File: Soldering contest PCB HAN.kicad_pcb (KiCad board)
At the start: 2 copper layers, 99.1 x 98.6 mm, 17 parts, among them J1 Screw_Terminal_01x02, Q1 2N3904, Q2 2N3904

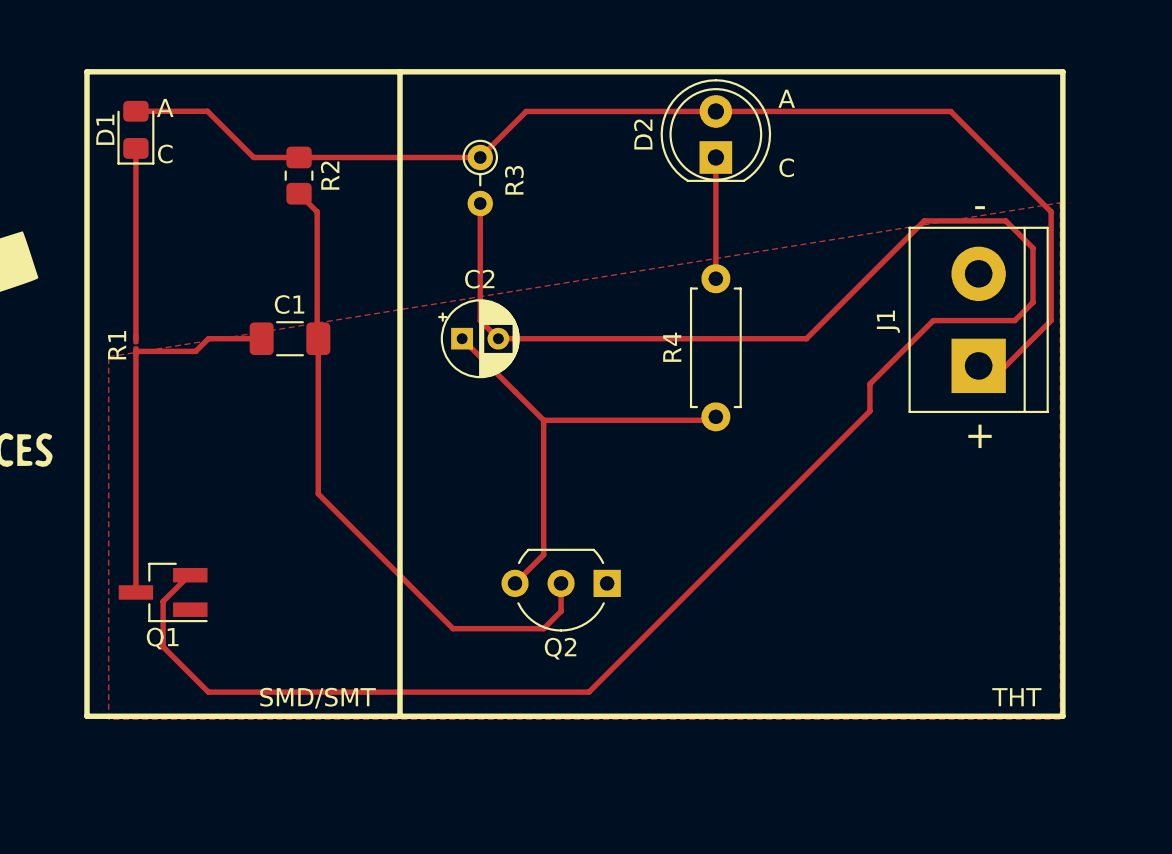
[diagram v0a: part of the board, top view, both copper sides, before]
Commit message: changed terminal position
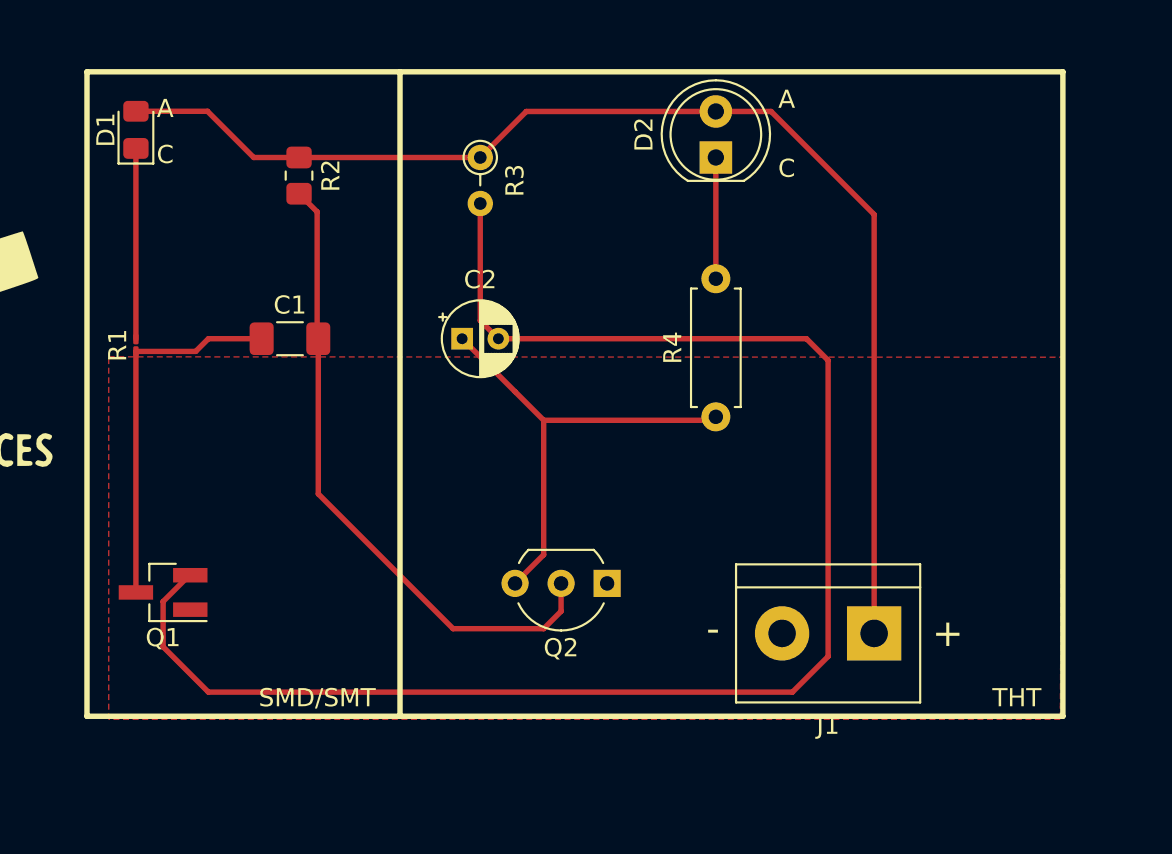
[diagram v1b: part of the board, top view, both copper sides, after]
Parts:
- moved J1 15.8 mm to (177.0, 111.8), turned to 180 degrees
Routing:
- net Net-(C2-Pad2): track 107.1 -> 86.0 mm
- net Net-(D1-Pad2): track 65.9 -> 68.3 mm
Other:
- board text added: "TIPS: -Wear safety goggles -Avoid breathing in the solder fumes -Use the appropriate soldering tip for the job -350°C-400°C are usual soldering temperatures -{dblquote}Pre tin{dblquote} components/wires -Heat the pad and the component while adding tin -Use a helping hand or board clamp -Pliers make handling small components easier -Solder paste requires around 220°C to melt -Low melt solder/hot a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"
- board text removed: "TIPS: -Wear safety goggles -Avoid breathing in the solder fumes -350°C-400°C are usual soldering temperatures -{dblquote}Pre tin{dblquote} components/wires -Heat the pad and the component while adding tin -Use a helping hand or board clamp -Pliers make handling small components easier -Solder paste requires around 220°C to melt -Low melt solder/hot air is the easiest way to remove components with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"
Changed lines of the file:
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@@
   )
   (footprint "TerminalBlock:TerminalBlock_bornier-2_P5.08mm" (layer "F.Cu")
-    (at 182.804 97 90)
+    (at 177.038 111.76 180)
     (descr "simple 2-pin terminal block, pitch 5.08mm, revamped version of bornier2")
     (tags "terminal block bornier2")
@@
     (property "Sheetname" "")
     (attr through_hole)
-    (fp_text reference "J1" (at 2.54 -5.08 90) (layer "F.SilkS")
+    (fp_text reference "J1" (at 2.54 -5.08) (layer "F.SilkS")
       (effects (font (size 1 1) (thickness 0.15)))
     )
-    (fp_text value "Screw_Terminal_01x02" (at 2.54 5.08 90) (layer "F.Fab")
+    (fp_text value "Screw_Terminal_01x02" (at 2.54 5.08) (layer "F.Fab")
       (effects (font (size 1 1) (thickness 0.15)))
     )
-    (fp_text user "${REFERENCE}" (at 2.54 0 90) (layer "F.Fab")
+    (fp_text user "${REFERENCE}" (at 2.54 0) (layer "F.Fab")
       (effects (font (size 1 1) (thickness 0.15)))
     )
@@
     (fp_line (start -2.46 3.75) (end 7.54 3.75) (layer "F.Fab") (width 0.1))
     (fp_line (start 7.54 3.75) (end 7.54 -3.75) (layer "F.Fab") (width 0.1))
-    (pad "1" thru_hole rect (at 0 0 90) (size 3 3) (drill 1.52) (layers *.Cu *.Mask)
+    (pad "1" thru_hole rect (at 0 0 180) (size 3 3) (drill 1.52) (layers *.Cu *.Mask)
       (net 6 "Net-(D1-Pad2)") (pinfunction "Pin_1") (pintype "passive"))
-    (pad "2" thru_hole circle (at 5.08 0 90) (size 3 3) (drill 1.52) (layers *.Cu *.Mask)
+    (pad "2" thru_hole circle (at 5.08 0 180) (size 3 3) (drill 1.52) (layers *.Cu *.Mask)
       (net 8 "GND") (pinfunction "Pin_2") (pintype "passive"))
     (model "${KICAD6_3DMODEL_DIR}/TerminalBlock.3dshapes/TerminalBlock_bornier-2_P5.08mm.wrl"
@@
   (gr_arc (start 205.486 51.301321) (mid 208.90322 52.71678) (end 210.318679 56.134) (layer "Edge.Cuts") (width 0.1))
   (gr_line (start 210.318679 56.134) (end 210.312 149.86) (layer "Edge.Cuts") (width 0.1))
-  (gr_text "TIPS:\n-Wear safety goggles\n-Avoid breathing in the solder fumes\n-350°C-400°C are usual soldering temperatures\n-{dblquote}Pre tin{dblquote} components/wires\n-Heat the pad and the component while adding tin\n-Use a helping hand or board clamp\n-Pliers make handling small components easier\n-Solder paste requires around 220°C to melt\n-Low melt solder/hot air is the easiest way to remove \n components with many pins\n-Dull solder joints aren't great\n" (at 208.788 72.644) (layer "B.SilkS")
+  (gr_text "TIPS:\n-Wear safety goggles\n-Avoid breathing in the solder fumes\n-Use the appropriate soldering tip for the job\n-350°C-400°C are usual soldering temperatures\n-{dblquote}Pre tin{dblquote} components/wires\n-Heat the pad and the component while adding tin\n-Use a helping hand or board clamp\n-Pliers make handling small components easier\n-Solder paste requires around 220°C to melt\n-Low melt solder/hot air is the easiest way to remove \n components with many pins\n-Avoid dull looking solder joints\n" (at 208.788 72.644) (layer "B.SilkS")
     (effects (font (size 1.2 1.2) (thickness 0.17)) (justify left mirror))
   )
@@
     (effects (font (size 1 1) (thickness 0.15)))
   )
-  (gr_text "-" (at 182.88 88.138) (layer "F.SilkS")
+  (gr_text "-" (at 168.148 111.506) (layer "F.SilkS")
     (effects (font (size 1.5 1.5) (thickness 0.2)))
   )
@@
     (effects (font (size 2 2) (thickness 0.3)))
   )
-  (gr_text "+\n" (at 182.88 100.838) (layer "F.SilkS")
+  (gr_text "+\n" (at 181.102 111.76) (layer "F.SilkS")
     (effects (font (size 1.5 1.5) (thickness 0.2)))
   )
@@
   (segment (start 158.804 100) (end 157.224 98.42) (width 0.3) (layer "F.Cu") (net 3))
   (segment (start 157.224 109) (end 158.804 107.42) (width 0.3) (layer "F.Cu") (net 3))
+  (segment (start 140.304 115) (end 137.804 112.5) (width 0.3) (layer "F.Cu") (net 4))
+  (segment (start 137.804 112.5) (end 137.804 110) (width 0.3) (layer "F.Cu") (net 4))
+  (segment (start 174.498 113.03) (end 172.528 115) (width 0.3) (layer "F.Cu") (net 4))
+  (segment (start 137.804 110) (end 139.254 108.55) (width 0.3) (layer "F.Cu") (net 4))
+  (segment (start 173.304 95.5) (end 174.498 96.694) (width 0.3) (layer "F.Cu") (net 4))
+  (segment (start 139.254 108.55) (end 139.304 108.55) (width 0.3) (layer "F.Cu") (net 4))
+  (segment (start 172.528 115) (end 140.304 115) (width 0.3) (layer "F.Cu") (net 4))
   (segment (start 156.304 95.5) (end 173.304 95.5) (width 0.3) (layer "F.Cu") (net 4))
-  (segment (start 185.804 93.5) (end 184.804 94.5) (width 0.3) (layer "F.Cu") (net 4))
-  (segment (start 139.254 108.55) (end 139.304 108.55) (width 0.3) (layer "F.Cu") (net 4))
-  (segment (start 184.804 94.5) (end 180.304 94.5) (width 0.3) (layer "F.Cu") (net 4))
-  (segment (start 180.304 94.5) (end 176.804 98) (width 0.3) (layer "F.Cu") (net 4))
-  (segment (start 184.304 89) (end 185.804 90.5) (width 0.3) (layer "F.Cu") (net 4))
-  (segment (start 176.804 98) (end 176.804 99.5) (width 0.3) (layer "F.Cu") (net 4))
-  (segment (start 173.304 95.5) (end 179.804 89) (width 0.3) (layer "F.Cu") (net 4))
-  (segment (start 176.804 99.5) (end 161.304 115) (width 0.3) (layer "F.Cu") (net 4))
-  (segment (start 140.304 115) (end 137.804 112.5) (width 0.3) (layer "F.Cu") (net 4))
   (segment (start 155.304 88.04) (end 155.304 94.5) (width 0.3) (layer "F.Cu") (net 4))
-  (segment (start 185.804 90.5) (end 185.804 93.5) (width 0.3) (layer "F.Cu") (net 4))
   (segment (start 155.304 94.5) (end 156.304 95.5) (width 0.3) (layer "F.Cu") (net 4))
-  (segment (start 137.804 110) (end 139.254 108.55) (width 0.3) (layer "F.Cu") (net 4))
-  (segment (start 161.304 115) (end 140.304 115) (width 0.3) (layer "F.Cu") (net 4))
-  (segment (start 179.804 89) (end 184.304 89) (width 0.3) (layer "F.Cu") (net 4))
-  (segment (start 137.804 112.5) (end 137.804 110) (width 0.3) (layer "F.Cu") (net 4))
+  (segment (start 174.498 96.694) (end 174.498 113.03) (width 0.3) (layer "F.Cu") (net 4))
   (segment (start 136.304 95.525) (end 136.304 85) (width 0.3) (layer "F.Cu") (net 5))
+  (segment (start 171.352 82.96) (end 177.038 88.646) (width 0.3) (layer "F.Cu") (net 6))
   (segment (start 145.304 85.5) (end 155.304 85.5) (width 0.3) (layer "F.Cu") (net 6))
   (segment (start 157.844 82.96) (end 155.304 85.5) (width 0.3) (layer "F.Cu") (net 6))
-  (segment (start 168.304 82.96) (end 181.264 82.96) (width 0.3) (layer "F.Cu") (net 6))
-  (segment (start 184.304 97) (end 182.804 97) (width 0.3) (layer "F.Cu") (net 6))
+  (segment (start 168.304 82.96) (end 171.352 82.96) (width 0.3) (layer "F.Cu") (net 6))
   (segment (start 168.304 82.96) (end 157.844 82.96) (width 0.3) (layer "F.Cu") (net 6))
   (segment (start 142.804 85.5) (end 145.304 85.5) (width 0.3) (layer "F.Cu") (net 6))
-  (segment (start 186.804 94.5) (end 184.304 97) (width 0.3) (layer "F.Cu") (net 6))
-  (segment (start 181.264 82.96) (end 186.804 88.5) (width 0.3) (layer "F.Cu") (net 6))
+  (segment (start 177.038 88.646) (end 177.038 111.76) (width 0.3) (layer "F.Cu") (net 6))
   (segment (start 140.254 82.95) (end 142.804 85.5) (width 0.3) (layer "F.Cu") (net 6))
-  (segment (start 186.804 88.5) (end 186.804 94.5) (width 0.3) (layer "F.Cu") (net 6))
   (segment (start 136.304 82.95) (end 140.254 82.95) (width 0.3) (layer "F.Cu") (net 6))
   (segment (start 168.304 92.19) (end 168.304 85.5) (width 0.3) (layer "F.Cu") (net 7))
@@
     (connect_pads (clearance 0.508))
     (min_thickness 0.254) (filled_areas_thickness no)
-    (fill yes (thermal_gap 0.508) (thermal_bridge_width 0.508))
+    (fill (thermal_gap 0.508) (thermal_bridge_width 0.508))
     (polygon
       (pts
@@
         (xy 134.804 116.5)
         (xy 134.804 96.5)
-        (xy 187.304 88)
+        (xy 187.452 96.52)
       )
     )

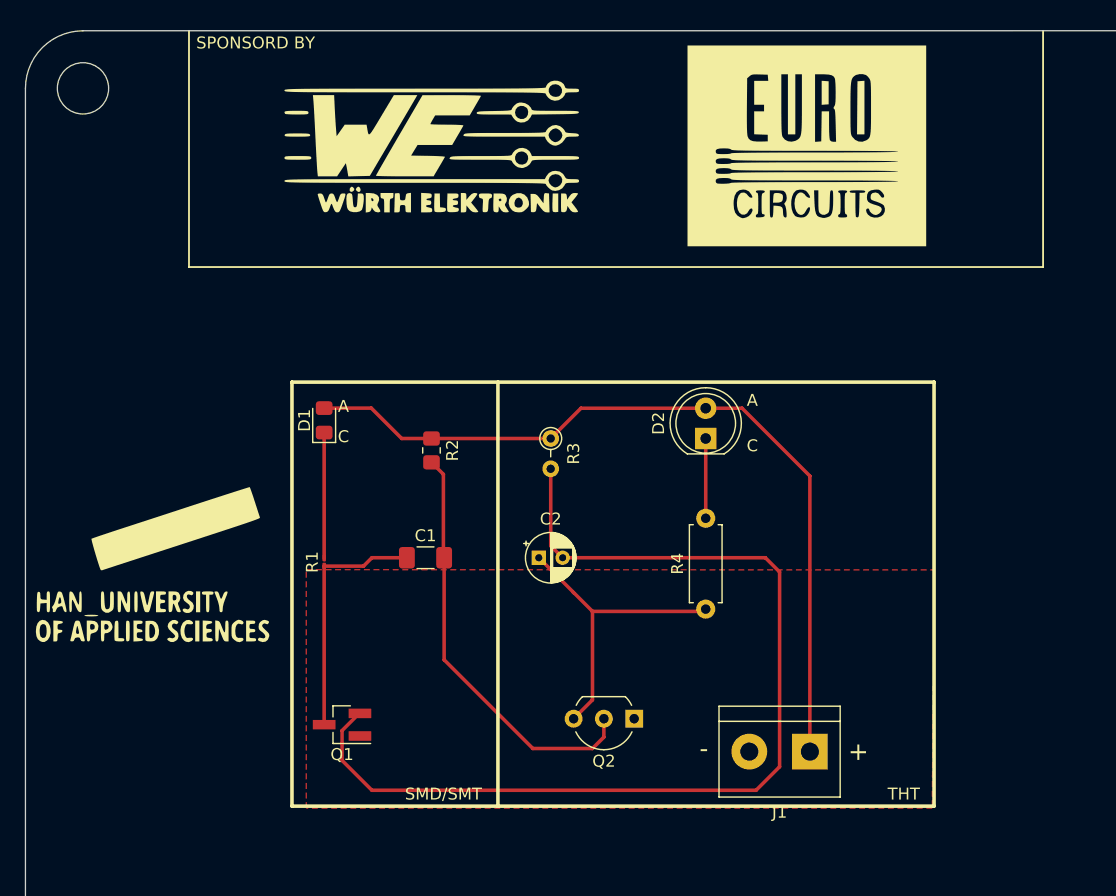
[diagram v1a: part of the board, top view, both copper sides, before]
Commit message: incorporated Remko's feedback
-added Romex logo
-added text: "Designed for: ESE-day 27 January 2023 soldering contest"
-moved terminal to mid bottom to balance weight
-
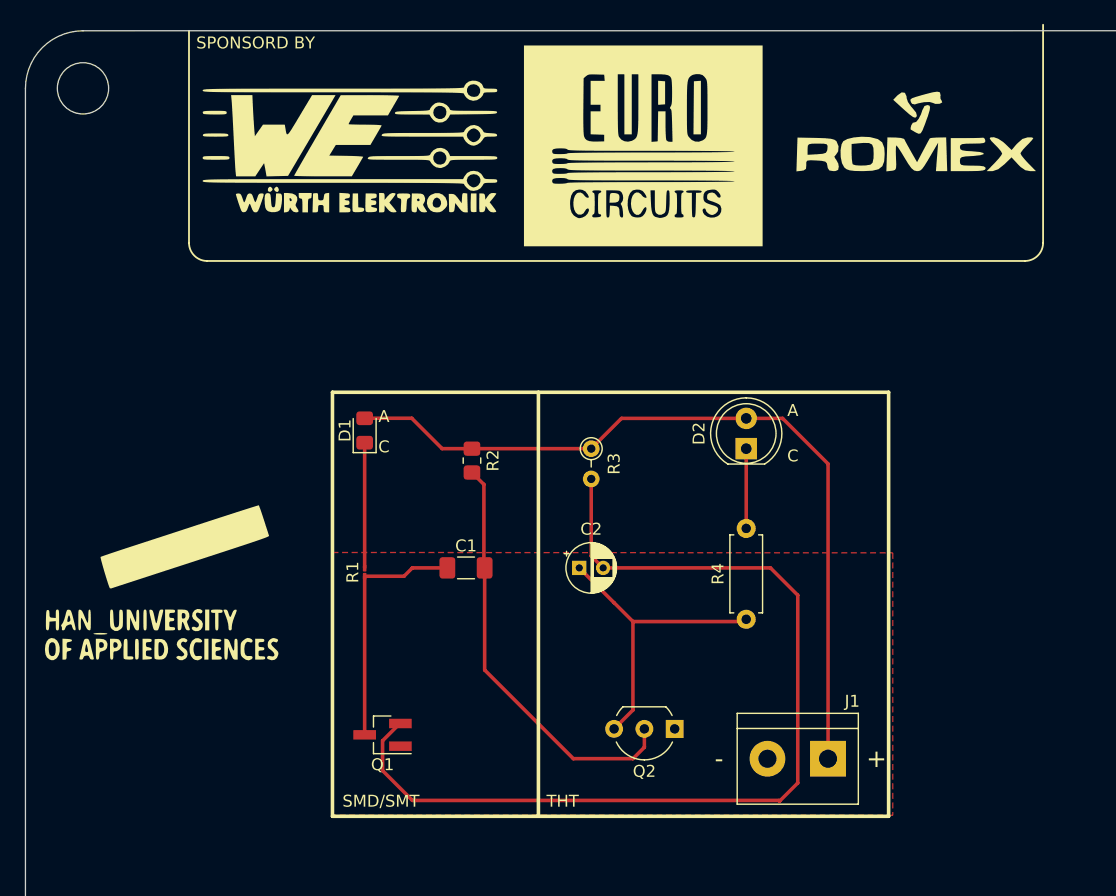
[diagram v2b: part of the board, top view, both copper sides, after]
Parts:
- added G***: LOGO, LOGO, F.Cu at (185.9, 59.7)
- moved G*** 13.7 mm to (163.1, 61.0)
- moved G*** 6.86 mm to (138.4, 61.0)
- moved C1 3.50 mm to (148.2, 96.4)
- moved C2 3.50 mm to (157.7, 96.4)
- moved D1 3.50 mm to (139.7, 84.8)
- moved D2 3.50 mm to (171.7, 86.4)
- moved Q1 3.50 mm to (141.2, 110.4)
- moved Q2 3.50 mm to (165.7, 109.9)
- moved R1 3.50 mm to (139.7, 96.7)
- moved R2 3.50 mm to (148.7, 87.4)
- moved R3 3.50 mm to (158.7, 86.4)
- moved R4 3.50 mm to (171.7, 100.7)
- moved G*** 1.70 mm to (122.7, 97.5)
- moved J1 1.64 mm to (178.6, 112.4)
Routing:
- net Net-(C2-Pad2): track 86.0 -> 82.0 mm
- net Net-(D1-Pad2): track 68.3 -> 67.3 mm
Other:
- board text added: "Project: Astable multivibrator Version: 0.1 Date: 18-11-2022 Designed for: ESE-day 27 January 2023 soldering contest Designed by: Casper R. Tak"
- board text removed: "Project: Astable multivibrator (soldering contest) Version: 0.1 Date: 18-11-2022 Designed by: Casper R. Tak"

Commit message: removed tips, added ESE txt
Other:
- board text added: "EMBEDDED SYSTEMS ENGINEERING"
- board text removed: "TIPS: -Wear safety goggles -Avoid breathing in the solder fumes -Use the appropriate soldering tip for the job -350°C-400°C are usual soldering temperatures -{dblquote}Pre tin{dblquote} components/wires -Heat the pad and the component while adding tin -Use a helping hand or board clamp -Pliers make handling small components easier -Solder paste requires around 220°C to melt -Low melt solder/hot a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"
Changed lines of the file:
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@@
   (gr_arc (start 205.486 51.301321) (mid 208.90322 52.71678) (end 210.318679 56.134) (layer "Edge.Cuts") (width 0.1))
   (gr_line (start 210.318679 56.134) (end 210.312 149.86) (layer "Edge.Cuts") (width 0.1))
-  (gr_text "TIPS:\n-Wear safety goggles\n-Avoid breathing in the solder fumes\n-Use the appropriate soldering tip for the job\n-350°C-400°C are usual soldering temperatures\n-{dblquote}Pre tin{dblquote} components/wires\n-Heat the pad and the component while adding tin\n-Use a helping hand or board clamp\n-Pliers make handling small components easier\n-Solder paste requires around 220°C to melt\n-Low melt solder/hot air is the easiest way to remove \n components with many pins\n-Avoid dull looking solder joints\n" (at 208.788 72.644) (layer "B.SilkS")
-    (effects (font (size 1.2 1.2) (thickness 0.17)) (justify left mirror))
+  (gr_text "EMBEDDED \nSYSTEMS \nENGINEERING" (at 206.248 71.12) (layer "B.SilkS")
+    (effects (font (size 3 3) (thickness 0.4)) (justify left mirror))
   )
-  (gr_text "Project: Astable multivibrator\nVersion: 0.1\nDate: 18-11-2022\nDesigned for: ESE-day 27 January 2023 soldering contest\nDesigned by: Casper R. Tak" (at 208.788 143.256) (layer "B.SilkS")
-    (effects (font (size 1.5 1.5) (thickness 0.2)) (justify left mirror))
+  (gr_text "Project: Astable multivibrator\nVersion: 0.1\nDate: 18-11-2022\nDesigned for: ESE-day 27 January 2023 soldering contest\nDesigned by: Casper R. Tak" (at 208.28 140.208) (layer "B.SilkS")
+    (effects (font (size 2 2) (thickness 0.3)) (justify left mirror))
   )
   (gr_text "SPONSORD BY" (at 130.556 52.324) (layer "F.SilkS")
